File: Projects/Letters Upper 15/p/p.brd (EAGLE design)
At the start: 16.5 x 21.6 mm, 42 parts

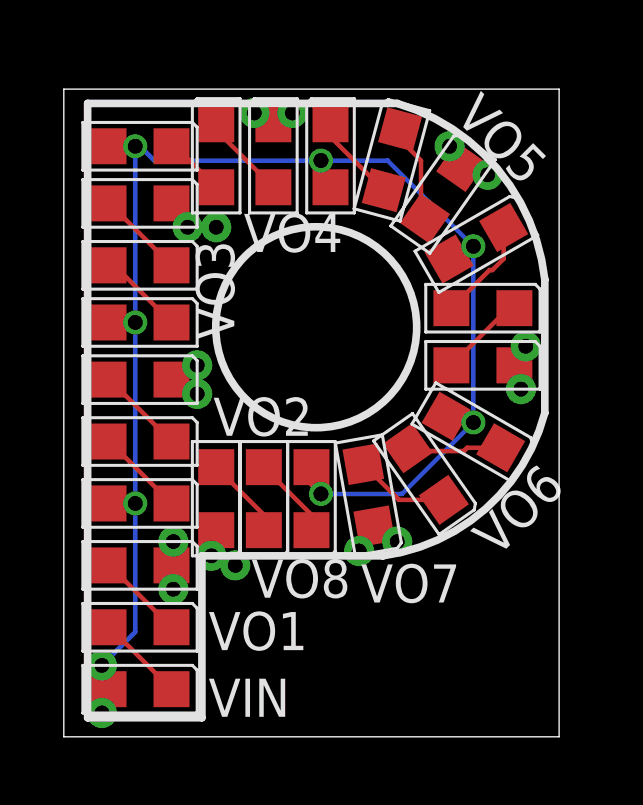
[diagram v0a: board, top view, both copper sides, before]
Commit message: 
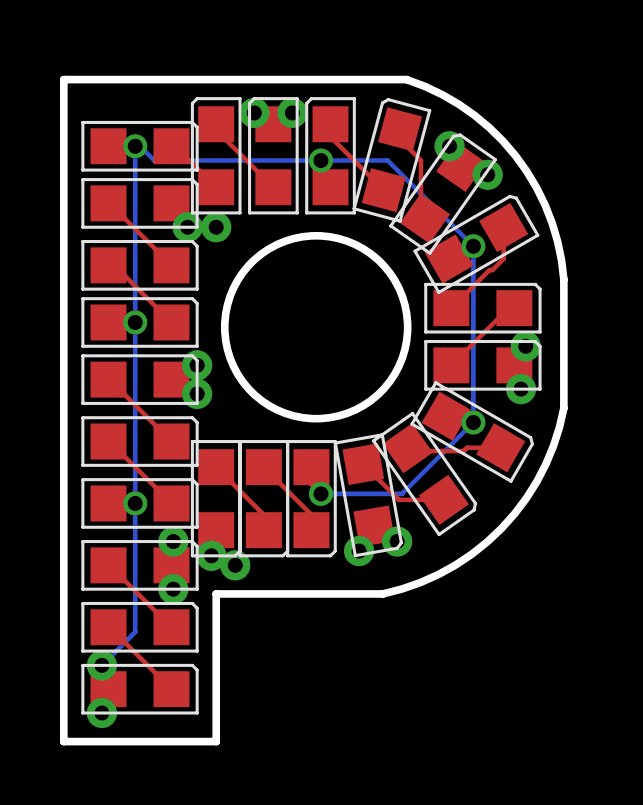
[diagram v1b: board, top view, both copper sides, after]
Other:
- board size 16.5 x 21.6 mm -> 16.7 x 22.1 mm
